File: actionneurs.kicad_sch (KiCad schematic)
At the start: 72 parts, among them J1 690367280876, J10 ESC_35_1_P, J11 690367280876, J12 ESC_35_2_S, J14 690367280876, J6 ESC_35_1_P, J7 RGBA_LEDs, J9 ESC_35_1_S, Q1 G2302, Q10 G2302, Q11 G2302, Q12 G2302, Q13 G2302, Q14 G2302, Q15 G2302, Q16 G2302, Q17 G2302, Q2 G2302, Q3 G2302, Q4 G2302, Q5 G2302, Q9 G2302

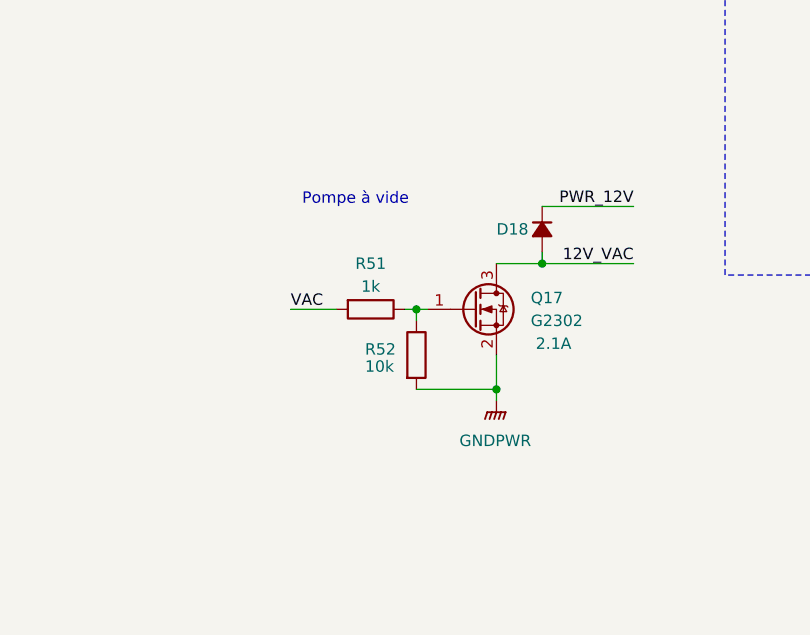
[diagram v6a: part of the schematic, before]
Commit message: Simplification arborescence schema, correction duplicate designator TODO: connect floating signal on MCU sheet, update routing, split the board in two
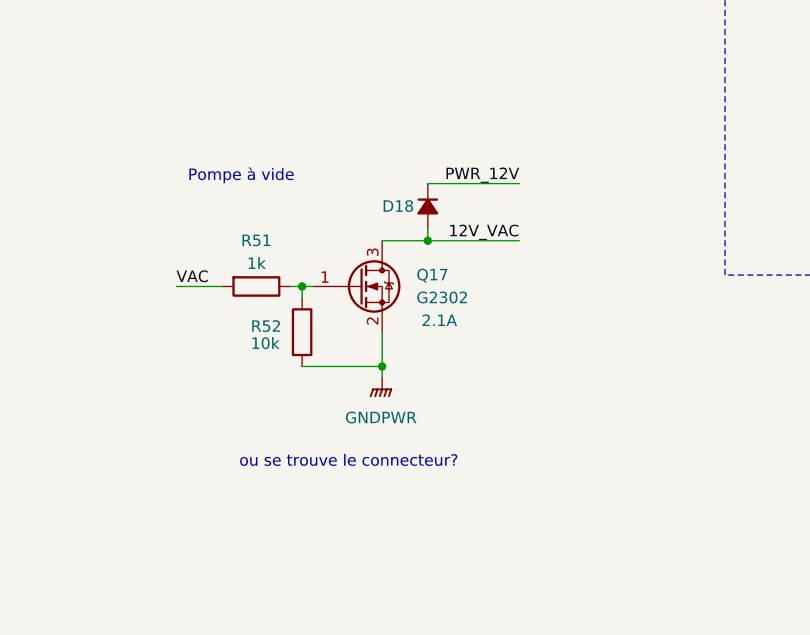
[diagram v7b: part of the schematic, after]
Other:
- note added: "ou se trouve le connecteur?"
- moved on the sheet: D18, Q17, R51, R52
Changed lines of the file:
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@@
 	)
 	(junction
-		(at 226.06 152.4)
+		(at 213.36 149.86)
 		(diameter 0)
 		(color 0 0 0 0)
@@
 	)
 	(junction
-		(at 217.17 143.51)
+		(at 204.47 140.97)
 		(diameter 0)
 		(color 0 0 0 0)
@@
 	)
 	(junction
-		(at 231.14 138.43)
+		(at 218.44 135.89)
 		(diameter 0)
 		(color 0 0 0 0)
@@
 	(wire
 		(pts
-			(xy 217.17 143.51) (xy 218.44 143.51)
+			(xy 204.47 140.97) (xy 205.74 140.97)
 		)
 		(stroke
@@
 	(wire
 		(pts
-			(xy 231.14 137.16) (xy 231.14 138.43)
+			(xy 218.44 134.62) (xy 218.44 135.89)
 		)
 		(stroke
@@
 	(wire
 		(pts
-			(xy 226.06 152.4) (xy 226.06 153.67)
+			(xy 213.36 149.86) (xy 213.36 151.13)
 		)
 		(stroke
@@
 	(wire
 		(pts
-			(xy 231.14 132.08) (xy 241.3 132.08)
+			(xy 218.44 129.54) (xy 228.6 129.54)
 		)
 		(stroke
@@
 	(wire
 		(pts
-			(xy 217.17 152.4) (xy 226.06 152.4)
+			(xy 204.47 149.86) (xy 213.36 149.86)
 		)
 		(stroke
@@
 	(wire
 		(pts
-			(xy 226.06 148.59) (xy 226.06 152.4)
+			(xy 213.36 146.05) (xy 213.36 149.86)
 		)
 		(stroke
@@
 	(wire
 		(pts
-			(xy 203.2 143.51) (xy 208.28 143.51)
+			(xy 190.5 140.97) (xy 195.58 140.97)
 		)
 		(stroke
@@
 	(wire
 		(pts
-			(xy 217.17 144.78) (xy 217.17 143.51)
+			(xy 204.47 142.24) (xy 204.47 140.97)
 		)
 		(stroke
@@
 	(wire
 		(pts
-			(xy 215.9 143.51) (xy 217.17 143.51)
+			(xy 203.2 140.97) (xy 204.47 140.97)
 		)
 		(stroke
@@
 	(wire
 		(pts
-			(xy 231.14 138.43) (xy 241.3 138.43)
+			(xy 218.44 135.89) (xy 228.6 135.89)
 		)
 		(stroke
@@
 	(wire
 		(pts
-			(xy 226.06 138.43) (xy 231.14 138.43)
+			(xy 213.36 135.89) (xy 218.44 135.89)
 		)
 		(stroke
@@
 		)
 	)
+	(text "ou se trouve le connecteur?"
+		(exclude_from_sim no)
+		(at 197.485 161.29 0)
+		(effects
+			(font
+				(size 1.27 1.27)
+				(color 255 0 0 1)
+			)
+			(justify left bottom)
+		)
+	)
 	(text "Contrôle LEDs adressables"
 		(exclude_from_sim no)
@@
 	(text "Pompe à vide"
 		(exclude_from_sim no)
-		(at 204.47 132.08 0)
+		(at 191.77 129.54 0)
 		(effects
 			(font
@@
 	)
 	(label "PWR_12V"
-		(at 241.3 132.08 180)
+		(at 228.6 129.54 180)
 		(effects
 			(font
@@
 	)
 	(label "VAC"
-		(at 203.2 143.51 0)
+		(at 190.5 140.97 0)
 		(effects
 			(font
@@
 	)
 	(label "12V_VAC"
-		(at 241.3 138.43 180)
+		(at 228.6 135.89 180)
 		(effects
 			(font
@@
 	(symbol
 		(lib_id "Device:D_Small_Filled")
-		(at 231.14 134.62 270)
+		(at 218.44 132.08 270)
 		(unit 1)
 		(exclude_from_sim no)
@@
 		(dnp no)
 		(property "Reference" "D18"
-			(at 226.06 134.62 90)
+			(at 213.36 132.08 90)
 			(effects
 				(font
@@
 		)
 		(property "Value" "~"
-			(at 226.06 135.89 90)
+			(at 213.36 133.35 90)
 			(effects
 				(font
@@
 		)
 		(property "Footprint" "Diode_SMD:D_SOD-123F"
-			(at 231.14 134.62 90)
+			(at 218.44 132.08 90)
 			(effects
 				(font
@@
 		)
 		(property "Datasheet" "~"
-			(at 231.14 134.62 90)
+			(at 218.44 132.08 90)
 			(effects
 				(font
@@
 		)
 		(property "Description" ""
-			(at 231.14 134.62 0)
+			(at 218.44 132.08 0)
 			(effects
 				(font
@@
 		)
 		(property "Sim.Device" "D"
-			(at 231.14 134.62 0)
+			(at 218.44 132.08 0)
 			(effects
 				(font
@@
 		)
 		(property "Sim.Pins" "1=K 2=A"
-			(at 231.14 134.62 0)
+			(at 218.44 132.08 0)
 			(effects
 				(font
@@
 	(symbol
 		(lib_id "Device:R")
-		(at 217.17 148.59 0)
+		(at 204.47 146.05 0)
 		(unit 1)
 		(exclude_from_sim no)
@@
 		(dnp no)
 		(property "Reference" "R52"
-			(at 211.455 147.955 0)
+			(at 198.755 145.415 0)
 			(effects
 				(font
@@
 		)
 		(property "Value" "10k"
-			(at 211.455 149.86 0)
+			(at 198.755 147.32 0)
 			(effects
 				(font
@@
 		)
 		(property "Footprint" "Resistor_SMD:R_0603_1608Metric"
-			(at 215.392 148.59 90)
+			(at 202.692 146.05 90)
 			(effects
 				(font
@@
 		)
 		(property "Datasheet" "~"
-			(at 217.17 148.59 0)
+			(at 204.47 146.05 0)
 			(effects
 				(font
@@
 		)
 		(property "Description" ""
-			(at 217.17 148.59 0)
+			(at 204.47 146.05 0)
 			(effects
 				(font
@@
 	(symbol
 		(lib_id "Device:Q_NMOS_GSD")
-		(at 223.52 143.51 0)
+		(at 210.82 140.97 0)
 		(unit 1)
 		(exclude_from_sim no)
@@
 		(dnp no)
 		(property "Reference" "Q17"
-			(at 229.87 142.24 0)
+			(at 217.17 139.7 0)
 			(effects
 				(font
@@
 		)
 		(property "Value" "G2302"
-			(at 229.87 144.78 0)
+			(at 217.17 142.24 0)
 			(effects
 				(font
@@
 		)
 		(property "Footprint" "Package_TO_SOT_SMD:SOT-23"
-			(at 228.6 140.97 0)
+			(at 215.9 138.43 0)
 			(effects
 				(font
@@
 		)
 		(property "Datasheet" "~"
-			(at 223.52 143.51 0)
+			(at 210.82 140.97 0)
 			(effects
 				(font
@@
 		)
 		(property "Description" ""
-			(at 223.52 143.51 0)
+			(at 210.82 140.97 0)
 			(effects
 				(font
@@
 		)
 		(property "Id" "2.1A"
-			(at 232.41 147.32 0)
+			(at 219.71 144.78 0)
 			(effects
 				(font
@@
 	(symbol
 		(lib_id "power:GNDPWR")
-		(at 226.06 153.67 0)
+		(at 213.36 151.13 0)
 		(unit 1)
 		(exclude_from_sim no)
@@
 		(fields_autoplaced yes)
 		(property "Reference" "#PWR016"
-			(at 226.06 158.75 0)
+			(at 213.36 156.21 0)
 			(effects
 				(font
@@
 		)
 		(property "Value" "GNDPWR"
-			(at 225.933 158.115 0)
+			(at 213.233 155.575 0)
 			(effects
 				(font
@@
 		)
 		(property "Footprint" ""
-			(at 226.06 154.94 0)
+			(at 213.36 152.4 0)
 			(effects
 				(font
@@
 		)
 		(property "Datasheet" ""
-			(at 226.06 154.94 0)
+			(at 213.36 152.4 0)
 			(effects
 				(font
@@
 		)
 		(property "Description" ""
-			(at 226.06 153.67 0)
+			(at 213.36 151.13 0)
 			(effects
 				(font
@@
 	(symbol
 		(lib_id "Device:R")
-		(at 212.09 143.51 270)
+		(at 199.39 140.97 270)
 		(unit 1)
 		(exclude_from_sim no)
@@
 		(fields_autoplaced yes)
 		(property "Reference" "R51"
-			(at 212.09 138.43 90)
+			(at 199.39 135.89 90)
 			(effects
 				(font
@@
 		)
 		(property "Value" "1k"
-			(at 212.09 140.97 90)
+			(at 199.39 138.43 90)
 			(effects
 				(font
@@
 		)
 		(property "Footprint" "Resistor_SMD:R_0603_1608Metric"
-			(at 212.09 141.732 90)
+			(at 199.39 139.192 90)
 			(effects
 				(font
@@
 		)
 		(property "Datasheet" "~"
-			(at 212.09 143.51 0)
+			(at 199.39 140.97 0)
 			(effects
 				(font
@@
 		)
 		(property "Description" ""
-			(at 212.09 143.51 0)
+			(at 199.39 140.97 0)
 			(effects
 				(font

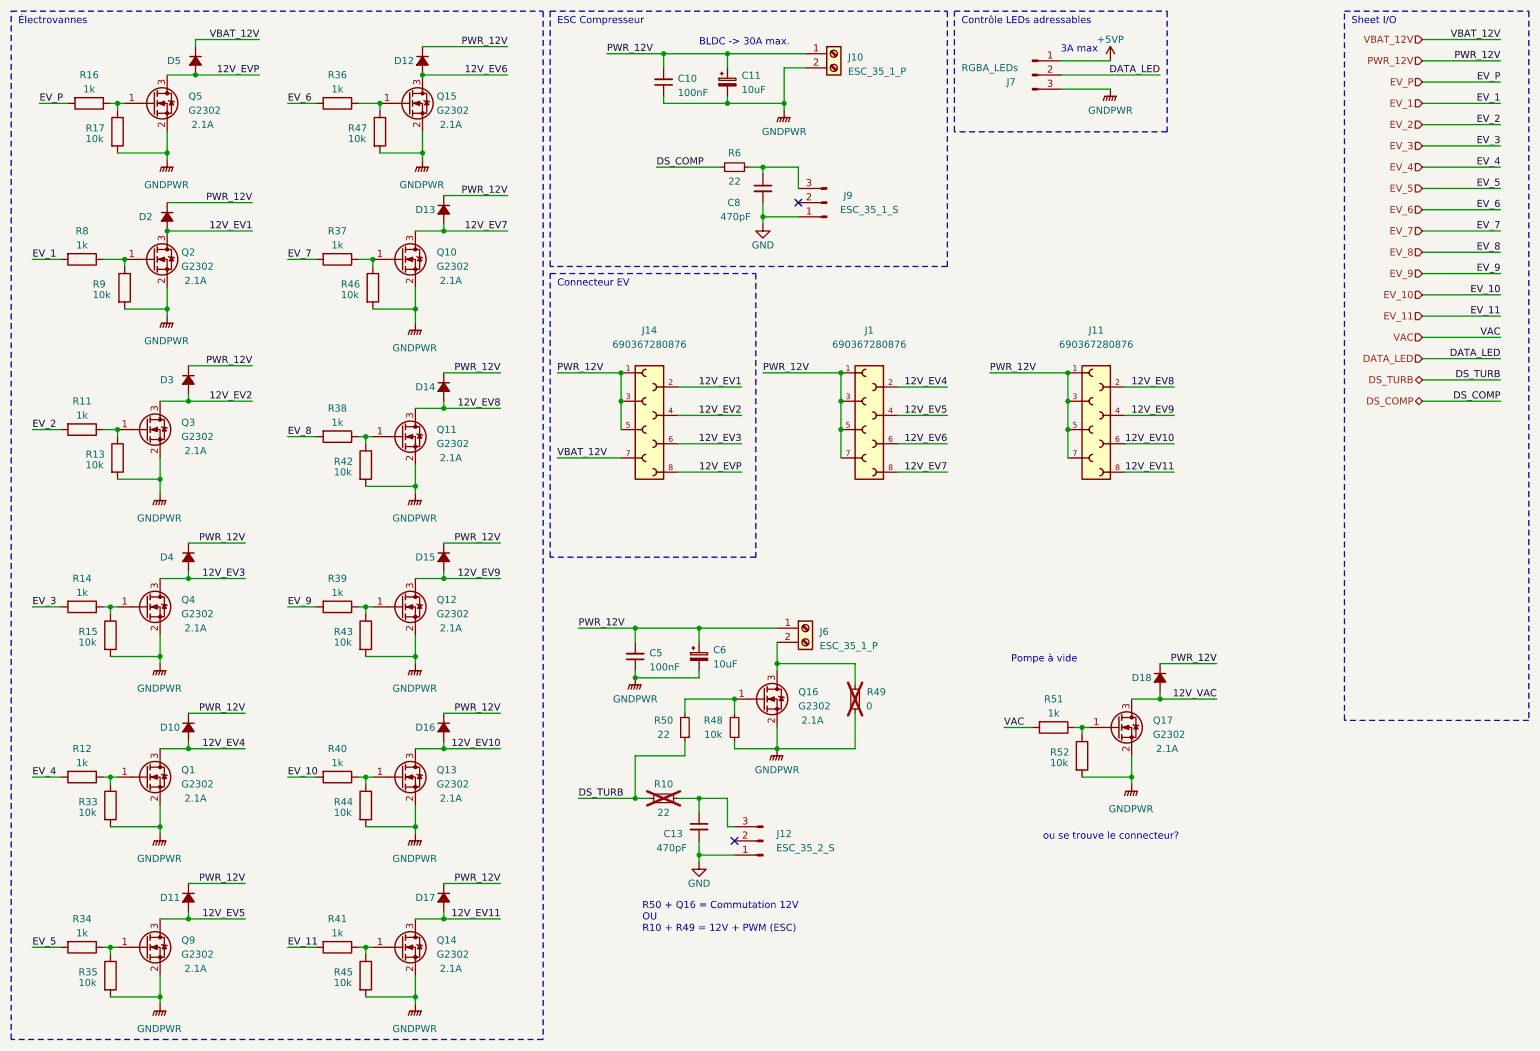
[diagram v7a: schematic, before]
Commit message: Correction de signaux non connectes, ajout de connecteur manquant, mise en forme du TOP
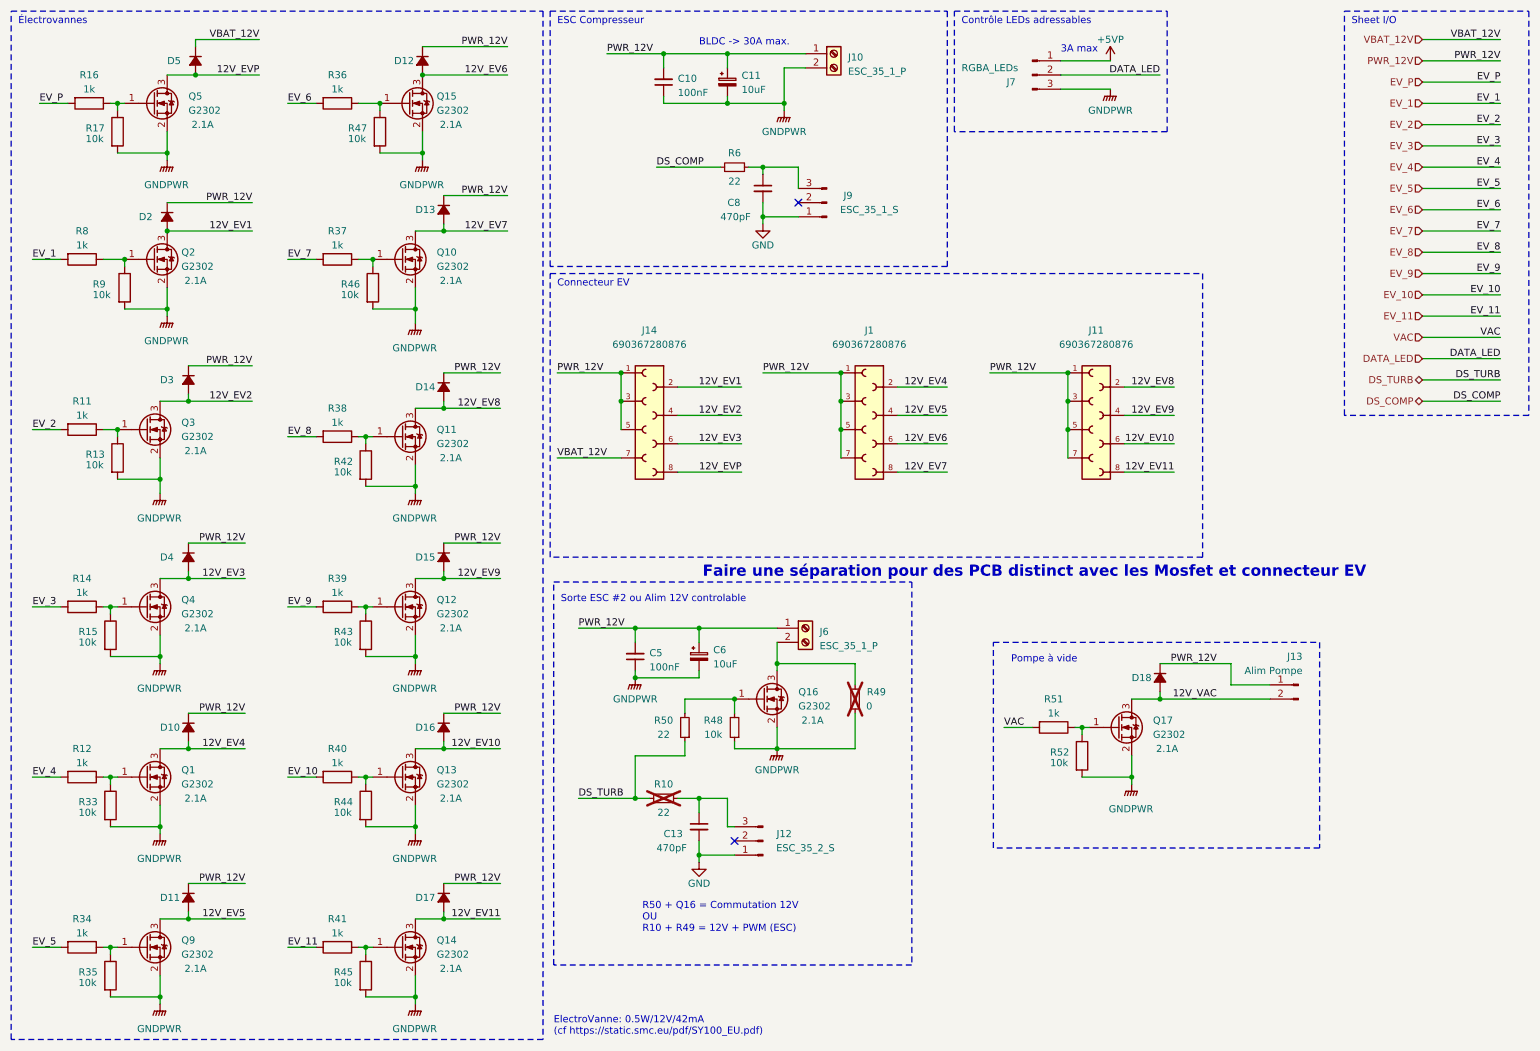
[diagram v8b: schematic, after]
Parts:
- added J13: Alim Pompe, Connector_PinHeader_2.54mm:PinHeader_1x02_P2.54mm_Vertical, symbol Connector:Conn_01x02_Pin
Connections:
- net 12V_VAC: now also J13.2 (Pin_2)
- net PWR_12V: now also J13.1 (Pin_1)
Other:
- note added: "ElectroVanne: 0.5W/12V/42mA (cf https://static.smc.eu/pdf/SY100_EU.pdf)"
- note added: "Faire une séparation pour des PCB distinct avec les Mosfet et connecteur EV"
- note added: "Sorte ESC #2 ou Alim 12V controlable"
- note removed: "ou se trouve le connecteur?"
